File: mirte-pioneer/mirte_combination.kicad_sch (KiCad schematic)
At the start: 49 parts, among them J1 Servo3, J10 IR1, J11 Conn_01x13_Female, J12 IR Object Detector 1, J14 IR2, J17 MC1, J18 MC2, J19 Servo1, J2 Conn_01x20_Female, J20 SRF1, J21 ENC2, J23 MC1-A, J24 MC1-B, J25 SRF2, J26 ENC1, J27 Servo2, J28 I2C2, J3 Servo4, J30 I2C1, J33 line out left, J34 Power in, J35 Power out, J37 on/off, J4 Conn_01x20_Female, J7 Keypad, J8 Conn_01x06_Female, J9 IR Object Detector 2, Q1 DMG2305UX, Q2 DMN2050L, SW1 on/off, U1 CH340C, U2 CH340E

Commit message: jlcpcb fixes mirte-pioneer
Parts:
- J34: footprint Connector_USB:USB_Micro-B_Molex-105017-0001 -> lcsc:MICRO-USB-SMD_U254-051T-4BH83-S1S; LCSC C456018 -> C319160
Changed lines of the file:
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@@
       (effects (font (size 1.27 1.27)) (justify left))
     )
-    (property "Footprint" "Connector_USB:USB_Micro-B_Molex-105017-0001" (at 240.03 64.77 0)
+    (property "Footprint" "lcsc:MICRO-USB-SMD_U254-051T-4BH83-S1S" (at 240.03 64.77 0)
       (effects (font (size 1.27 1.27)) hide)
     )
@@
       (effects (font (size 1.27 1.27)) hide)
     )
-    (property "LCSC" "C456018" (at 238.76 68.58 0)
+    (property "LCSC" "C319160" (at 238.76 68.58 0)
       (effects (font (size 1.27 1.27)) hide)
     )

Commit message: Change obj detector to 5V, add header for usb (lego)
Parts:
- added J5: Conn_01x06_Pin, Connector_PinHeader_2.54mm:PinHeader_1x06_P2.54mm_Vertical, symbol Connector:Conn_01x06_Pin
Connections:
- net 3V3: now also J12.1 (Pin_1), J9.1 (Pin_1)
- net 5V: now also J5.1 (Pin_1); no longer J12.1 (Pin_1), J9.1 (Pin_1)
- net D+: now also J5.4 (Pin_4)
- net D-: now also J5.3 (Pin_3)
- net D_GND: now also J5.2 (Pin_2)
- net usb-dm3: now also J5.5 (Pin_5)
- net usb-dp3: now also J5.6 (Pin_6)
- no-connect marks 19 -> 21
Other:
- note added: "pins for jst xh extension"
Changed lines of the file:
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@@
   (no_connect (at 241.3 60.96))
   (no_connect (at 81.28 167.64))
+  (no_connect (at 172.72 165.1))
   (no_connect (at 81.28 180.34))
   (no_connect (at 212.09 123.19))
@@
   (no_connect (at 212.09 118.11))
   (no_connect (at 191.77 113.03))
+  (no_connect (at 172.72 173.99))
   (no_connect (at 191.77 67.31))
   (no_connect (at 238.76 60.96))
@@
     (stroke (width 0) (type default))
   )
-  (polyline (pts (xy 99.06 142.24) (xy 17.78 142.24))
+  (polyline (pts (xy 111.76 142.24) (xy 17.78 142.24))
     (stroke (width 0) (type default))
   )
@@
     (stroke (width 0) (type default))
   )
-  (polyline (pts (xy 99.06 190.5) (xy 99.06 142.24))
+  (polyline (pts (xy 111.76 190.5) (xy 111.76 142.24))
     (stroke (width 0) (type default))
   )
@@
     (stroke (width 0) (type default))
   )
+  (wire (pts (xy 97.79 162.56) (xy 81.28 162.56))
+    (stroke (width 0) (type default))
+  )
   (polyline (pts (xy 227.33 93.98) (xy 278.13 93.98))
     (stroke (width 0) (type default))
@@
     (stroke (width 0) (type default))
   )
+  (wire (pts (xy 97.79 157.48) (xy 81.28 157.48))
+    (stroke (width 0) (type default))
+  )
   (polyline (pts (xy 118.11 43.18) (xy 121.92 43.18))
     (stroke (width 0) (type default))
@@
     (stroke (width 0) (type default))
   )
+  (wire (pts (xy 97.79 165.1) (xy 81.28 165.1))
+    (stroke (width 0) (type default))
+  )
+  (wire (pts (xy 97.79 154.94) (xy 81.28 154.94))
+    (stroke (width 0) (type default))
+  )
   (polyline (pts (xy 227.33 17.78) (xy 227.33 90.17))
     (stroke (width 0) (type default))
@@
     (stroke (width 0) (type default))
   )
+  (wire (pts (xy 97.79 160.02) (xy 81.28 160.02))
+    (stroke (width 0) (type default))
+  )
   (wire (pts (xy 147.32 154.94) (xy 147.32 157.48))
     (stroke (width 0) (type default))
   )
+  (wire (pts (xy 97.79 152.4) (xy 81.28 152.4))
+    (stroke (width 0) (type default))
+  )
   (polyline (pts (xy 55.88 118.11) (xy 17.78 118.11))
     (stroke (width 0) (type default))
@@
     (stroke (width 0) (type default))
   )
-  (polyline (pts (xy 17.78 190.5) (xy 99.06 190.5))
+  (polyline (pts (xy 17.78 190.5) (xy 111.76 190.5))
     (stroke (width 0) (type default))
   )
@@
   (text "Servo 3" (at 114.3 123.19 0)
     (effects (font (size 1.27 1.27)) (justify right bottom))
+  )
+  (text "pins for jst xh extension" (at 91.44 171.45 0)
+    (effects (font (size 1.27 1.27)) (justify left bottom))
   )
   (text "Raspberry pico\n" (at 121.92 138.43 0)
@@
     )
   )
-  (global_label "5V" (shape input) (at 30.48 124.46 180) (fields_autoplaced)
-    (effects (font (size 1.27 1.27)) (justify right))
-    (property "Intersheetrefs" "${INTERSHEET_REFS}" (at -25.4 7.62 0)
-      (effects (font (size 1.27 1.27)) hide)
-    )
-  )
   (global_label "GP14" (shape input) (at 87.63 55.88 180) (fields_autoplaced)
     (effects (font (size 1.27 1.27)) (justify right))
@@
     )
   )
+  (global_label "3V3" (shape input) (at 54.61 124.46 180) (fields_autoplaced)
+    (effects (font (size 1.27 1.27)) (justify right))
+    (property "Intersheetrefs" "${INTERSHEET_REFS}" (at 48.6893 124.3806 0)
+      (effects (font (size 1.27 1.27)) (justify right) hide)
+    )
+  )
   (global_label "GP13" (shape input) (at 111.76 69.85 180) (fields_autoplaced)
     (effects (font (size 1.27 1.27)) (justify right))
@@
     (effects (font (size 1.27 1.27)) (justify right))
     (property "Intersheetrefs" "${INTERSHEET_REFS}" (at 72.7588 154.8606 0)
+      (effects (font (size 1.27 1.27)) (justify right) hide)
+    )
+  )
+  (global_label "3V3" (shape input) (at 30.48 124.46 180) (fields_autoplaced)
+    (effects (font (size 1.27 1.27)) (justify right))
+    (property "Intersheetrefs" "${INTERSHEET_REFS}" (at 24.5593 124.3806 0)
       (effects (font (size 1.27 1.27)) (justify right) hide)
     )
@@
     (property "Intersheetrefs" "${INTERSHEET_REFS}" (at 158.9979 54.5306 0)
       (effects (font (size 1.27 1.27)) (justify right) hide)
-    )
-  )
-  (global_label "5V" (shape input) (at 54.61 124.46 180) (fields_autoplaced)
-    (effects (font (size 1.27 1.27)) (justify right))
-    (property "Intersheetrefs" "${INTERSHEET_REFS}" (at 17.78 7.62 0)
-      (effects (font (size 1.27 1.27)) hide)
     )
   )
@@
         )
       )
+    )
+  )
+  (symbol (lib_id "Connector:Conn_01x06_Pin") (at 102.87 157.48 0) (mirror y) (unit 1)
+    (in_bom yes) (on_board yes) (dnp no)
+    (property "Reference" "J5" (at 104.14 157.48 0)
+      (effects (font (size 1.27 1.27)) (justify right))
+    )
+    (property "Value" "Conn_01x06_Pin" (at 95.25 167.64 0)
+      (effects (font (size 1.27 1.27)) (justify right))
+    )
+    (property "Footprint" "Connector_PinHeader_2.54mm:PinHeader_1x06_P2.54mm_Vertical" (at 102.87 157.48 0)
+      (effects (font (size 1.27 1.27)) hide)
+    )
+    (property "Datasheet" "~" (at 102.87 157.48 0)
+      (effects (font (size 1.27 1.27)) hide)
+    )
+    (pin "4")
+    (pin "3")
+    (pin "6")
+    (pin "1")
+    (pin "2")
+    (pin "5")
+    (instances
+      (project "mirte_combination"
+        (path "/76b487fd-45a4-4e6a-8af9-b4f78fb0af77"
+          (reference "J5") (unit 1)
+        )
+      )

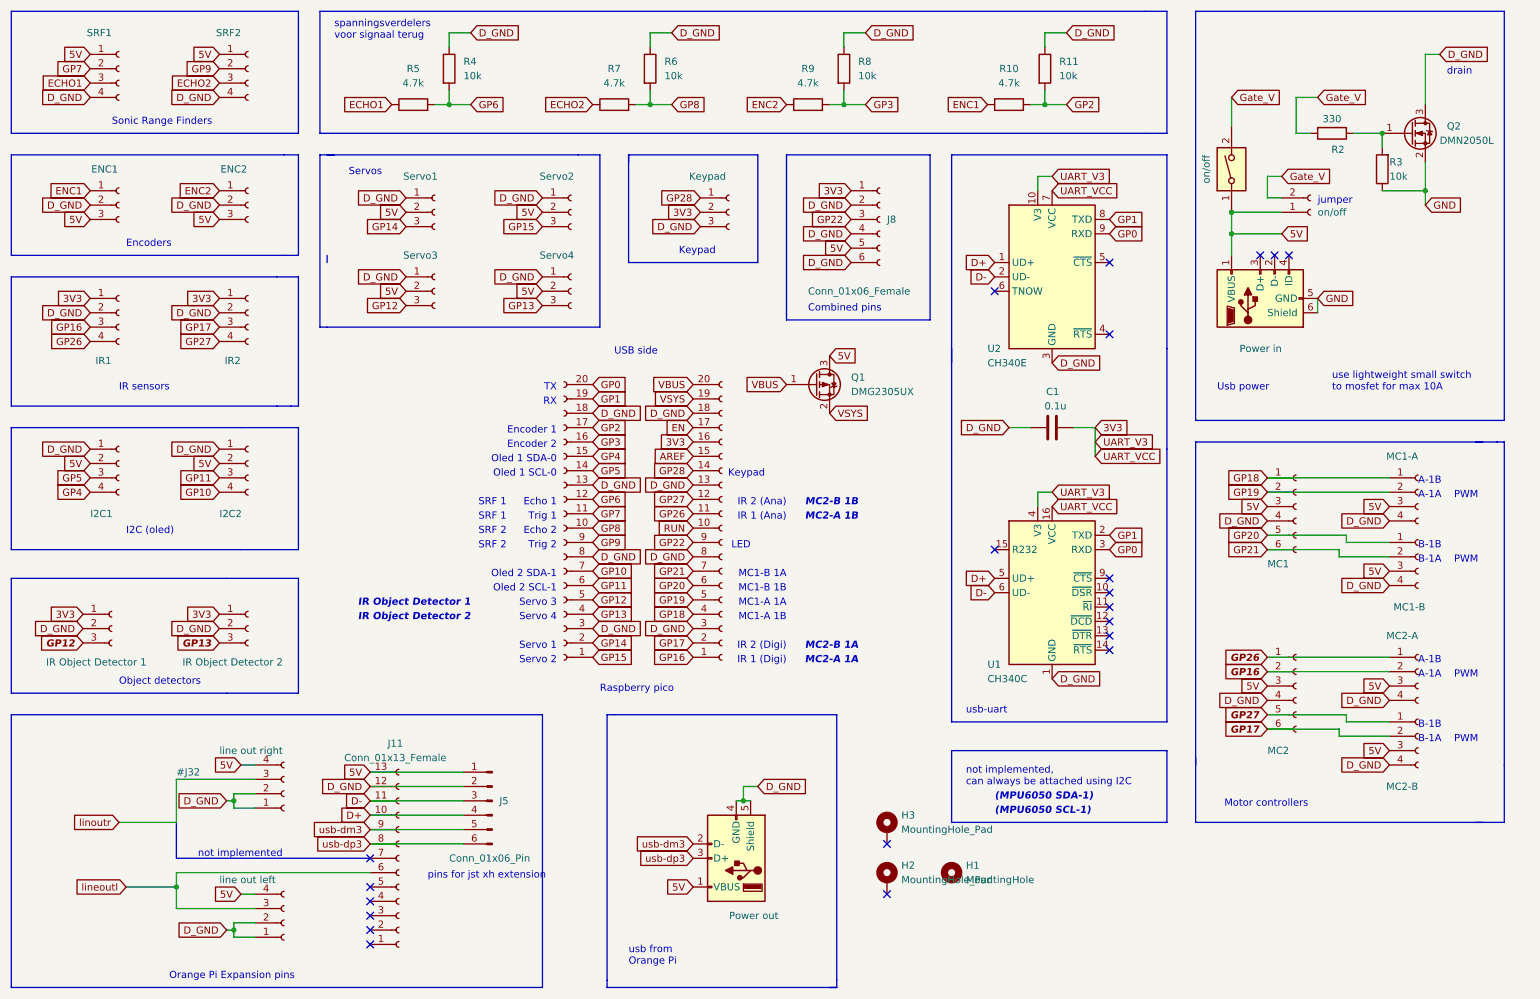
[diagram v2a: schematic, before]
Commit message: update version8, uart, usb c, usb switch
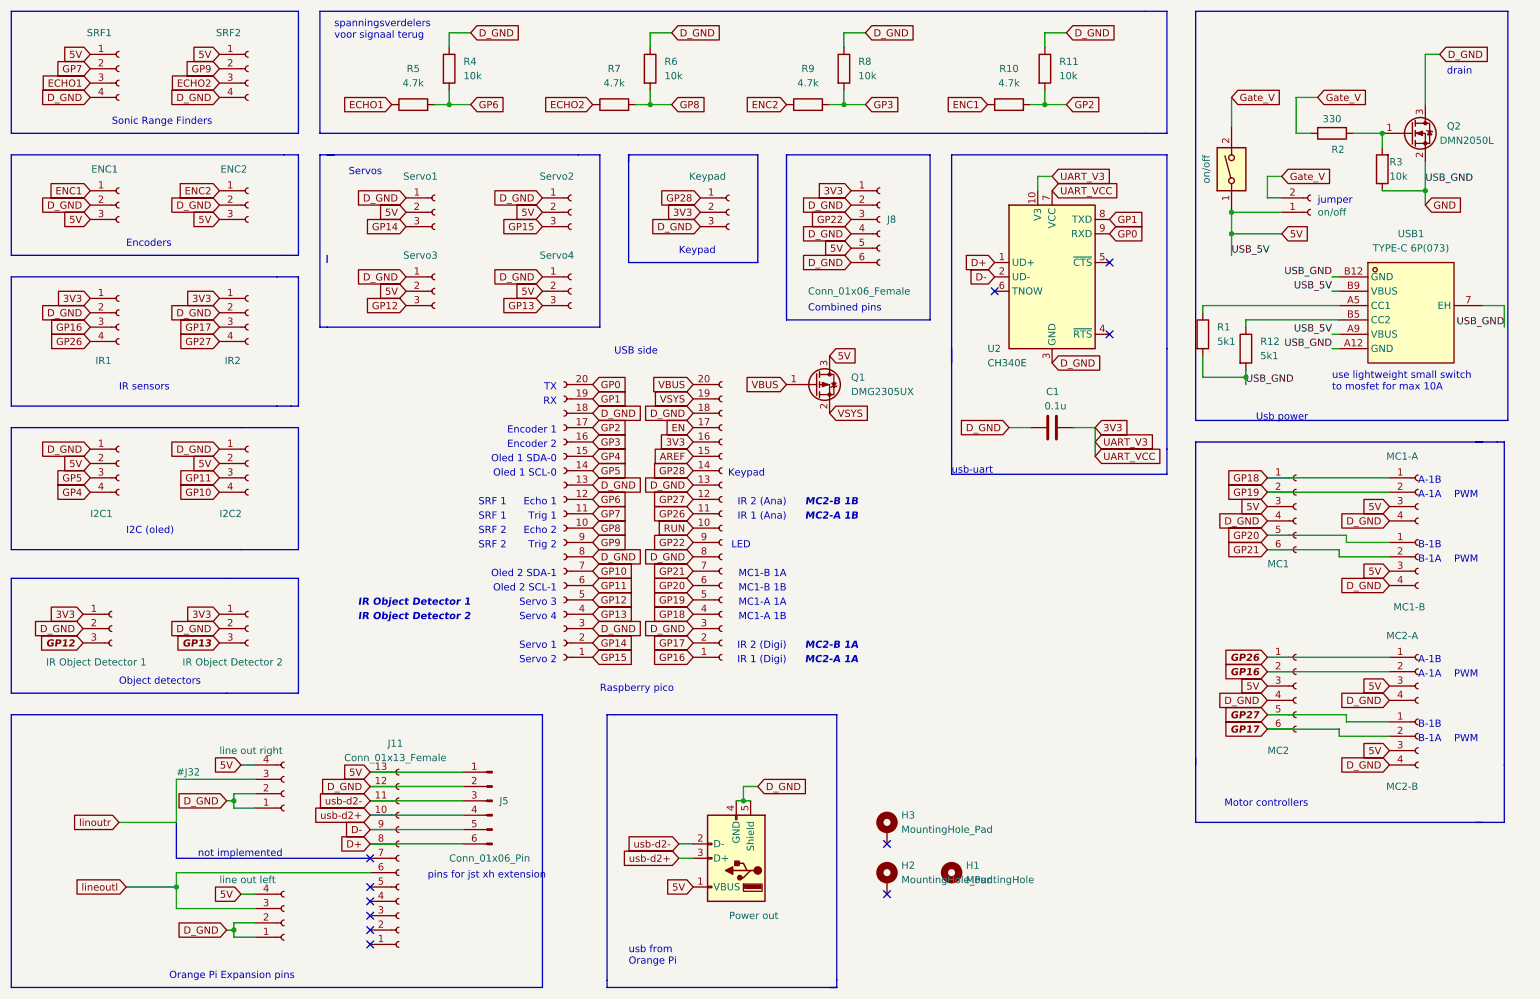
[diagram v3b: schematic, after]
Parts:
- removed J34: Power in, lcsc:MICRO-USB-SMD_U254-051T-4BH83-S1S, symbol test_pcb-rescue:USB_B_Micro-Connector
- removed U1: CH340C, Package_SO:SOIC-16_3.9x9.9mm_P1.27mm, symbol Interface_USB:CH340C
- added R1, R12: 5k1, Resistor_SMD:R_0805_2012Metric, symbol Device:R
- added USB1: TYPE-C 6P(073), lcsc:TYPE-C-SMD_TYPE-C-6P_5, symbol lcsc:TYPE-C6P(073)
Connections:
- net 5V: now also USB1.A9 (VBUS), USB1.B9 (VBUS)
- net D+: now also J11.8 (Pin_8), J5.6 (Pin_6); no longer J11.10 (Pin_10), J5.4 (Pin_4)
- net D-: now also J11.9 (Pin_9), J5.5 (Pin_5); no longer J11.11 (Pin_11), J5.3 (Pin_3)
- net GND: now also R1.2, R12.2, USB1.7 (EH), USB1.A12 (GND), USB1.B12 (GND)
- removed net usb-dm3: J11.9 (Pin_9), J35.2 (D-), J5.5 (Pin_5)
- removed net usb-dp3: J11.8 (Pin_8), J35.3 (D+), J5.6 (Pin_6)
- new net: R1.1, USB1.A5 (CC1)
- new net: R12.1, USB1.B5 (CC2)
- new net usb-d2+: J11.10 (Pin_10), J35.3 (D+), J5.4 (Pin_4)
- new net usb-d2-: J11.11 (Pin_11), J35.2 (D-), J5.3 (Pin_3)
- no-connect marks 21 -> 11
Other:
- note removed: "(MPU6050 SCL-1)"
- note removed: "(MPU6050 SDA-1)"
- note removed: "not implemented, can always be attached using I2C"

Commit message: change switch
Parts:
- removed SW1: on/off, Button_Switch_THT:SW_Slide_1P2T_CK_OS102011MS2Q, symbol Switch:SW_DIP_x01
- added SW2: SK12D07VG5, lcsc:SW-TH_SK12D07VG5, symbol lcsc:SK12D07VG5
- R1, R12: LCSC (none) -> C27834
- USB1: LCSC (none) -> C668623
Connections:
- net 5V: now also SW2.1
- net Gate_V: now also SW2.2
- no-connect marks 11 -> 14
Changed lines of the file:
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@@
 	)
 	(junction
-		(at 233.68 53.34)
-		(diameter 0)
-		(color 0 0 0 0)
-	)
-	(junction
 		(at 130.81 34.29)
 		(diameter 0)
@@
 	)
 	(junction
+		(at 233.68 53.34)
+		(diameter 0)
+		(color 0 0 0 0)
+	)
+	(junction
 		(at 165.1 34.29)
 		(diameter 0)
@@
 	)
 	(no_connect
+		(at 229.87 30.48)
+	)
+	(no_connect
 		(at 172.72 165.1)
 	)
 	(no_connect
+		(at 237.49 30.48)
+	)
+	(no_connect
 		(at 81.28 180.34)
 	)
@@
 	)
 	(no_connect
+		(at 240.03 30.48)
+	)
+	(no_connect
 		(at 81.28 172.72)
 	)
@@
 	(wire
 		(pts
+			(xy 232.41 30.48) (xy 232.41 53.34)
+		)
+		(stroke
+			(width 0)
+			(type default)
+		)
+	)
+	(wire
+		(pts
 			(xy 236.22 82.55) (xy 236.22 83.82)
 		)
@@
 	(wire
 		(pts
+			(xy 232.41 53.34) (xy 233.68 53.34)
+		)
+		(stroke
+			(width 0)
+			(type default)
+		)
+	)
+	(wire
+		(pts
 			(xy 92.71 34.29) (xy 95.25 34.29)
 		)
@@
 	(wire
 		(pts
+			(xy 234.95 30.48) (xy 234.95 35.56)
+		)
+		(stroke
+			(width 0)
+			(type default)
+		)
+	)
+	(wire
+		(pts
 			(xy 236.22 72.39) (xy 236.22 73.66)
 		)
@@
 		)
 	)
-	(wire
-		(pts
-			(xy 233.68 33.02) (xy 233.68 38.1)
-		)
-		(stroke
-			(width 0)
-			(type default)
-		)
-	)
 	(polyline
 		(pts
@@
 	(global_label "Gate_V"
 		(shape input)
-		(at 233.68 33.02 0)
+		(at 234.95 35.56 0)
 		(fields_autoplaced yes)
 		(effects
@@
 		)
 		(property "Intersheetrefs" "${INTERSHEET_REFS}"
-			(at 242.3826 33.0994 0)
+			(at 243.6526 35.6394 0)
 			(effects
 				(font
@@
 	)
 	(symbol
+		(lib_id "lcsc:SK12D07VG5")
+		(at 234.95 25.4 0)
+		(unit 1)
+		(exclude_from_sim no)
+		(in_bom yes)
+		(on_board yes)
+		(dnp no)
+		(fields_autoplaced yes)
+		(property "Reference" "SW2"
+			(at 241.3 20.3199 0)
+			(effects
+				(font
+					(size 1.27 1.27)
+				)
+				(justify left)
+			)
+		)
+		(property "Value" "SK12D07VG5"
+			(at 241.3 22.8599 0)
+			(effects
+				(font
+					(size 1.27 1.27)
+				)
+				(justify left)
+			)
+		)
+		(property "Footprint" "lcsc:SW-TH_SK12D07VG5"
+			(at 234.95 38.1 0)
+			(effects
+				(font
+					(size 1.27 1.27)
+				)
+				(hide yes)
+			)
+		)
+		(property "Datasheet" "https://lcsc.com/product-detail/Toggle-Switches_SHOU-HAN-SK12D07VG5_C431548.html"
+			(at 234.95 40.64 0)
+			(effects
+				(font
+					(size 1.27 1.27)
+				)
+				(hide yes)
+			)
+		)
+		(property "Description" ""
+			(at 234.95 25.4 0)
+			(effects
+				(font
+					(size 1.27 1.27)
+				)
+				(hide yes)
+			)
+		)
+		(property "LCSC Part" "C431548"
+			(at 234.95 43.18 0)
+			(effects
+				(font
+					(size 1.27 1.27)
+				)
+				(hide yes)
+			)
+		)
+		(pin "2"
+		)
+		(pin "1"
+		)
+		(pin "3"
+		)
+		(pin "4"
+		)
+		(pin "5"
+		)
+		(instances
+			(project ""
+				(path "/76b487fd-45a4-4e6a-8af9-b4f78fb0af77"
+					(reference "SW2")
+					(unit 1)
+				)
+			)
+		)
+	)
+	(symbol
 		(lib_id "Device:R")
 		(at 165.1 27.94 0)
@@
 			)
 		)
+		(property "LCSC" "C668623"
+			(at 265.43 57.15 0)
+			(effects
+				(font
+					(size 1.27 1.27)
+				)
+				(hide yes)
+			)
+		)
 		(pin "A9"
 		)
@@
 			)
 		)
+		(property "LCSC" "C27834"
+			(at 231.14 73.6599 0)
+			(effects
+				(font
+					(size 1.27 1.27)
+				)
+				(hide yes)
+			)
+		)
 		(pin "1"
 		)
@@
 	)
 	(symbol
-		(lib_id "Switch:SW_DIP_x01")
-		(at 233.68 45.72 90)
-		(unit 1)
-		(exclude_from_sim no)
-		(in_bom yes)
-		(on_board yes)
-		(dnp no)
-		(property "Reference" "SW1"
-			(at 226.8982 45.72 0)
-			(effects
-				(font
-					(size 1.27 1.27)
-				)
-				(hide yes)
-			)
-		)
-		(property "Value" "on/off"
-			(at 229.2096 45.72 0)
-			(effects
-				(font
-					(size 1.27 1.27)
-				)
-			)
-		)
-		(property "Footprint" "Button_Switch_THT:SW_Slide_1P2T_CK_OS102011MS2Q"
-			(at 229.235 45.72 0)
-			(effects
-				(font
-					(size 1.27 1.27)
-				)
-				(hide yes)
-			)
-		)
-		(property "Datasheet" "~"
-			(at 233.68 45.72 0)
-			(effects
-				(font
-					(size 1.27 1.27)
-				)
-				(hide yes)
-			)
-		)
-		(property "Description" ""
-			(at 233.68 45.72 0)
-			(effects
-				(font
-					(size 1.27 1.27)
-				)
-				(hide yes)
-			)
-		)
-		(property "Farnell_num" "1201431"
-			(at 233.68 45.72 0)
-			(effects
-				(font
-					(size 1.27 1.27)
-				)
-				(hide yes)
-			)
-		)
-		(property "Manufacturer" "C&K COMPONENTS"
-			(at 233.68 45.72 0)
-			(effects
-				(font
-					(size 1.27 1.27)
-				)
-				(hide yes)
-			)
-		)
-		(property "Manufacturer_num" "OS102011MA1QN1"
-			(at 233.68 45.72 0)
-			(effects
-				(font
-					(size 1.27 1.27)
-				)
-				(hide yes)
-			)
-		)
-		(property "remarks" ""
-			(at 233.68 45.72 0)
-			(effects
-				(font
-					(size 1.27 1.27)
-				)
-				(hide yes)
-			)
-		)
-		(property "farnell_alternative" ""
-			(at 233.68 45.72 0)
-			(effects
-				(font
-					(size 1.27 1.27)
-				)
-				(hide yes)
-			)
-		)
-		(property "LCSC" "C226259"
-			(at 233.68 45.72 0)
-			(effects
-				(font
-					(size 1.27 1.27)
-				)
-				(hide yes)
-			)
-		)
-		(pin "1"
-		)
-		(pin "2"
-		)
-		(instances
-			(project "mirte_combination"
-				(path "/76b487fd-45a4-4e6a-8af9-b4f78fb0af77"
-					(reference "SW1")
-					(unit 1)
-				)
-			)
-		)
-	)
-	(symbol
 		(lib_id "Device:R")
 		(at 124.46 34.29 90)
@@
 			(effects
 				(font
+					(size 1.27 1.27)
+				)
+				(hide yes)
+			)
+		)
+		(property "LCSC" "C27834"
+			(at 238.76 76.1999 0)
+			(effects
+				(font
